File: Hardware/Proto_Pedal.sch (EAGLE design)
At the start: 124 parts, among them Q1 2.5A/30V

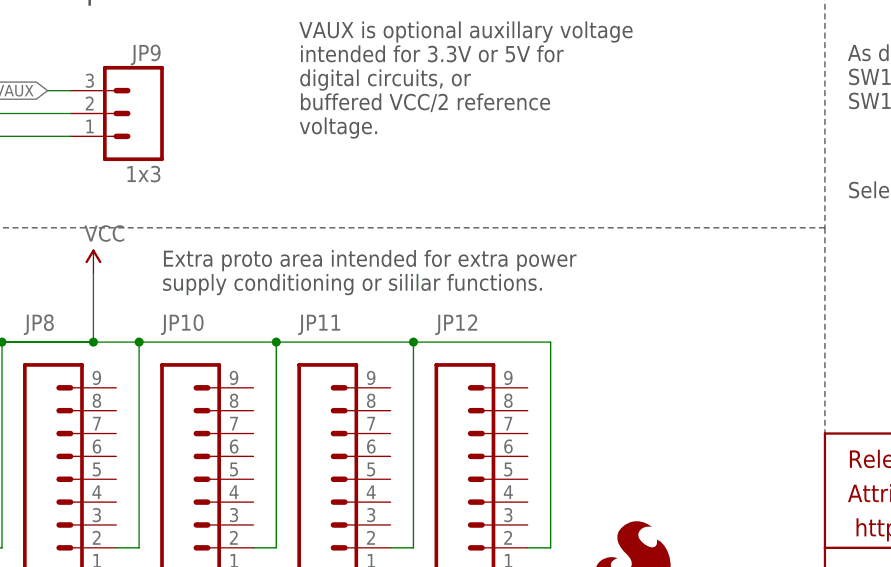
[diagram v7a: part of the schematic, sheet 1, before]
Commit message: A couple of fixes after review.
Fixed spelling of sililar.
One piece of top silk had fallen to bottom - now corrected.
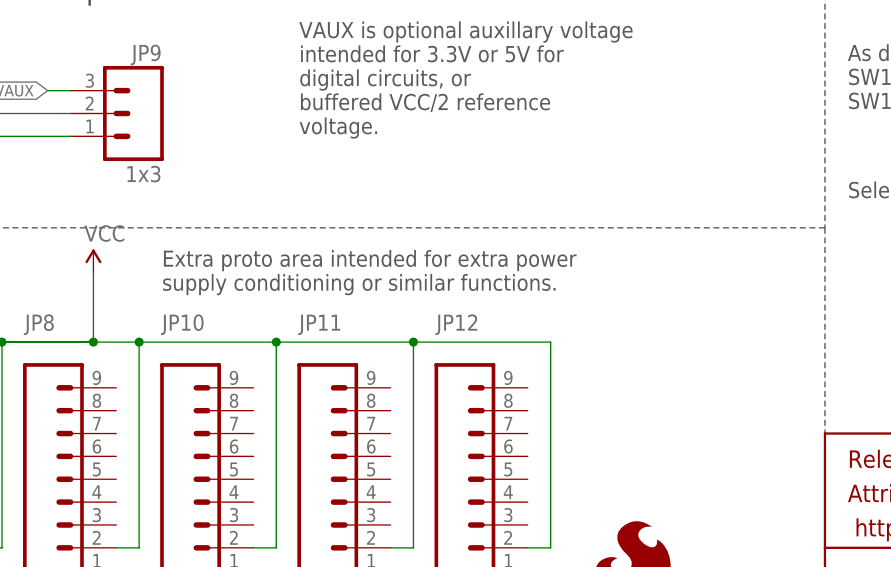
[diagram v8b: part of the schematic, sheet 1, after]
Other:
- note added: "Extra proto area intended for extra power supply conditioning or similar functions."
- note removed: "Extra proto area intended for extra power supply conditioning or sililar functions."
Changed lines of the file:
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@@
 voltage.</text>
 <text x="73.66" y="55.88" size="1.778" layer="97" font="vector" align="top-left">Extra proto area intended for extra power
-supply conditioning or sililar functions.</text>
+supply conditioning or similar functions.</text>
 <text x="88.9" y="109.22" size="1.778" layer="97" font="vector" align="top-left">C1 is input coupling cap
 C2 is output coupling cap.
